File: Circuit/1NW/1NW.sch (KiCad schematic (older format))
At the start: 30 parts, among them IC1 PIC16F18857-I_SP, J1 Conn_01x14_Female, J2 Conn_01x14_Female, J3 S8B-XH-A-1_LF__SN_, J4 S8B-XH-A-1_LF__SN_, U1 MAX485E

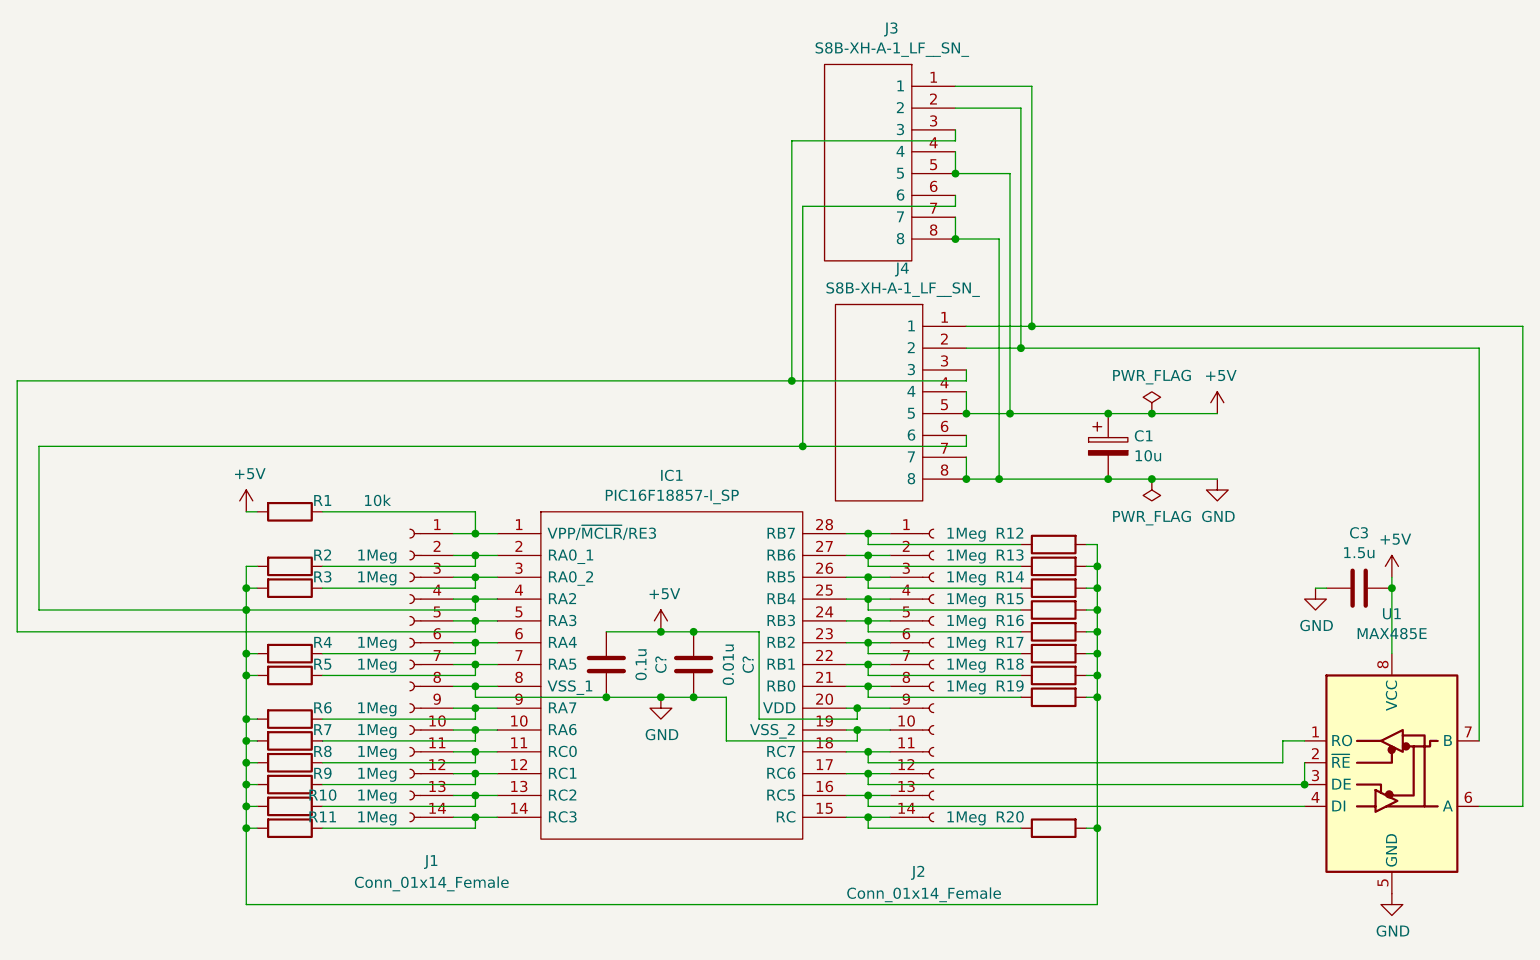
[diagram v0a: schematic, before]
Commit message: 8bit circuit (chip#0-5) complete
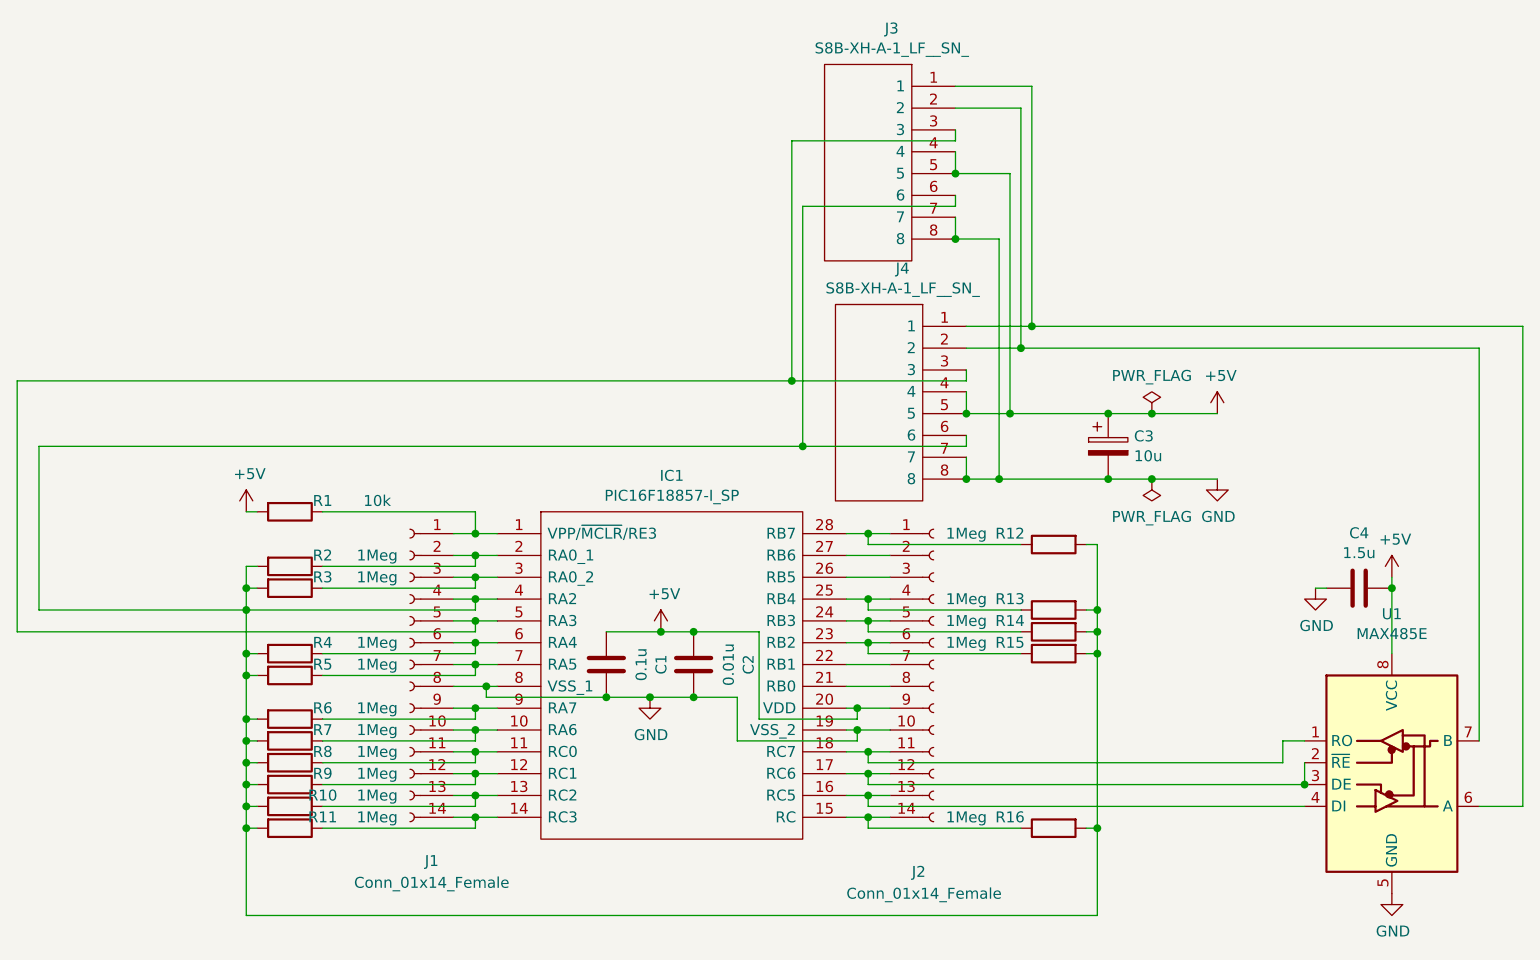
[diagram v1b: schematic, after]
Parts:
- removed C?: 0.1u, symbol Device:C
- removed C?: 0.01u, symbol Device:C
- removed R13, R14, R18, R19: 1Meg, symbol Device:R
- added C1: 0.1u, symbol Device:C
- added C2: 0.01u, symbol Device:C
- renumbered C1 to C3, C3 to C4, R15 to R13, R16 to R14, R17 to R15, R20 to R16
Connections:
- net +5V: now also C1.2, C2.2
- net GND: now also C1.1, C2.1
